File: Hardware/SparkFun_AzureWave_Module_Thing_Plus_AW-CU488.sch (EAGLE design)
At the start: 54 parts, among them J3 QWIIC_RA, J5 USB-C, Q1 2.5A/30V, U2 CP210X, U3 AP2112, U4 MCP73831, U5 TC7USB40MU

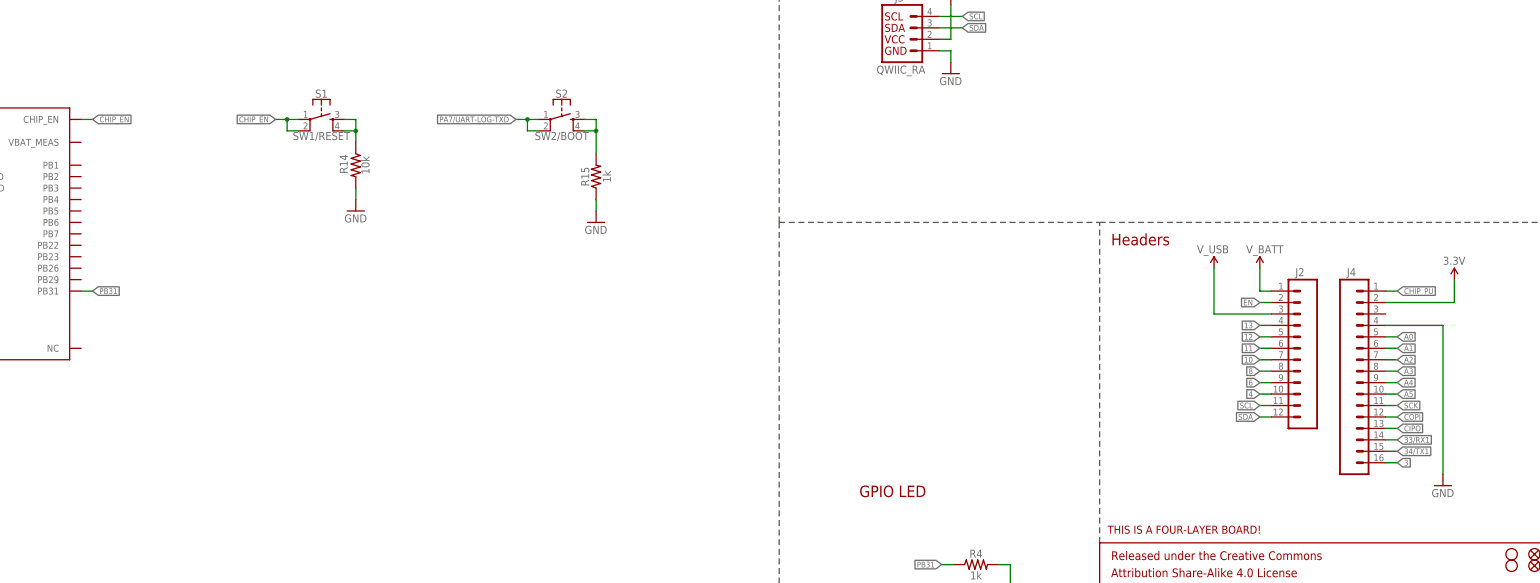
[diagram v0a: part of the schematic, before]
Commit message: vbat meas connection and some net cleanup
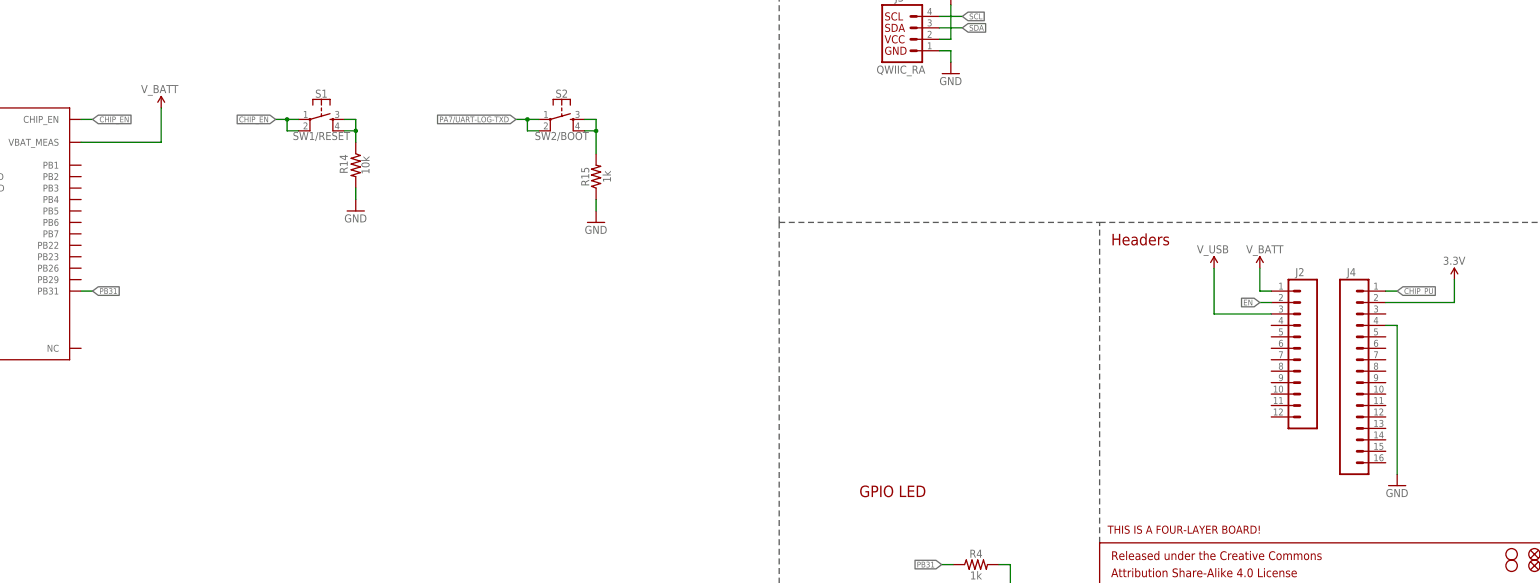
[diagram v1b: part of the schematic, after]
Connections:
- removed net 10: J2.7
- removed net 11: J2.6
- removed net 12: J2.5
- removed net 13: J2.4
- removed net 3: J4.16
- removed net 33/RX1: J4.14
- removed net 34/TX1: J4.15
- removed net 4: J2.10
- removed net 6: J2.9
- removed net 8: J2.8
- removed net A0: J4.5
- removed net A1: J4.6
- removed net A2: J4.7
- removed net A3: J4.8
- removed net A4: J4.9
- removed net A5: J4.10
- removed net CIPO: J4.13
- removed net COPI: J4.12
- removed net SCK: J4.11
- net SCL: no longer J2.11
- net SDA: no longer J2.12
- net V_BATT: now also U$13.VBAT_MEAS
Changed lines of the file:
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@@
 <part name="GND25" library="SparkFun-Aesthetics" deviceset="GND" device=""/>
 <part name="SUPPLY16" library="SparkFun-Aesthetics" deviceset="3.3V" device=""/>
+<part name="SUPPLY13" library="SparkFun-Aesthetics" deviceset="V_BATT" device=""/>
 </parts>
 <sheets>
@@
 <attribute name="VALUE" x="406.4" y="97.282" size="1.778" layer="96" font="vector"/>
 </instance>
-<instance part="GND2" gate="1" x="406.4" y="48.26" smashed="yes">
-<attribute name="VALUE" x="403.86" y="45.72" size="1.778" layer="96" font="vector"/>
+<instance part="GND2" gate="1" x="396.24" y="48.26" smashed="yes">
+<attribute name="VALUE" x="393.7" y="45.72" size="1.778" layer="96" font="vector"/>
 </instance>
 <instance part="C1" gate="G$1" x="101.6" y="226.06" smashed="yes">
@@
 <instance part="SUPPLY16" gate="G$1" x="45.72" y="144.78" smashed="yes">
 <attribute name="VALUE" x="44.704" y="148.336" size="1.778" layer="96" font="vector"/>
+</instance>
+<instance part="SUPPLY13" gate="G$1" x="121.92" y="132.08" smashed="yes" rot="MR0">
+<attribute name="VALUE" x="125.73" y="135.382" size="1.778" layer="96" font="vector" rot="MR0"/>
 </instance>
 </instances>
@@
 <pinref part="J4" gate="G$1" pin="4"/>
 <pinref part="GND2" gate="1" pin="GND"/>
-<wire x1="393.7" y1="83.82" x2="406.4" y2="83.82" width="0.1524" layer="91"/>
-<wire x1="406.4" y1="83.82" x2="406.4" y2="50.8" width="0.1524" layer="91"/>
+<wire x1="393.7" y1="83.82" x2="396.24" y2="83.82" width="0.1524" layer="91"/>
+<wire x1="396.24" y1="83.82" x2="396.24" y2="50.8" width="0.1524" layer="91"/>
 </segment>
 <segment>
@@
 <wire x1="365.76" y1="91.44" x2="365.76" y2="96.52" width="0.1524" layer="91"/>
 </segment>
+<segment>
+<pinref part="SUPPLY13" gate="G$1" pin="V_BATT"/>
+<wire x1="121.92" y1="132.08" x2="121.92" y2="124.46" width="0.1524" layer="91"/>
+<pinref part="U$13" gate="G$1" pin="VBAT_MEAS"/>
+<wire x1="121.92" y1="124.46" x2="104.14" y2="124.46" width="0.1524" layer="91"/>
+</segment>
 </net>
 <net name="N$1" class="0">
@@
 </segment>
 </net>
-<net name="A0" class="0">
-<segment>
-<pinref part="J4" gate="G$1" pin="5"/>
-<wire x1="393.7" y1="81.28" x2="396.24" y2="81.28" width="0.1524" layer="91"/>
-<label x="396.24" y="81.28" size="1.27" layer="95" font="vector" xref="yes"/>
-</segment>
-</net>
-<net name="A1" class="0">
-<segment>
-<pinref part="J4" gate="G$1" pin="6"/>
-<wire x1="393.7" y1="78.74" x2="396.24" y2="78.74" width="0.1524" layer="91"/>
-<label x="396.24" y="78.74" size="1.27" layer="95" font="vector" xref="yes"/>
-</segment>
-</net>
-<net name="A2" class="0">
-<segment>
-<pinref part="J4" gate="G$1" pin="7"/>
-<wire x1="393.7" y1="76.2" x2="396.24" y2="76.2" width="0.1524" layer="91"/>
-<label x="396.24" y="76.2" size="1.27" layer="95" font="vector" xref="yes"/>
-</segment>
-</net>
-<net name="A3" class="0">
-<segment>
-<pinref part="J4" gate="G$1" pin="8"/>
-<wire x1="393.7" y1="73.66" x2="396.24" y2="73.66" width="0.1524" layer="91"/>
-<label x="396.24" y="73.66" size="1.27" layer="95" font="vector" xref="yes"/>
-</segment>
-</net>
-<net name="A4" class="0">
-<segment>
-<pinref part="J4" gate="G$1" pin="9"/>
-<wire x1="393.7" y1="71.12" x2="396.24" y2="71.12" width="0.1524" layer="91"/>
-<label x="396.24" y="71.12" size="1.27" layer="95" font="vector" xref="yes"/>
-</segment>
-</net>
-<net name="A5" class="0">
-<segment>
-<pinref part="J4" gate="G$1" pin="10"/>
-<wire x1="393.7" y1="68.58" x2="396.24" y2="68.58" width="0.1524" layer="91"/>
-<label x="396.24" y="68.58" size="1.27" layer="95" font="vector" xref="yes"/>
-</segment>
-</net>
-<net name="SCK" class="0">
-<segment>
-<pinref part="J4" gate="G$1" pin="11"/>
-<wire x1="393.7" y1="66.04" x2="396.24" y2="66.04" width="0.1524" layer="91"/>
-<label x="396.24" y="66.04" size="1.27" layer="95" font="vector" xref="yes"/>
-</segment>
-</net>
-<net name="COPI" class="0">
-<segment>
-<pinref part="J4" gate="G$1" pin="12"/>
-<wire x1="393.7" y1="63.5" x2="396.24" y2="63.5" width="0.1524" layer="91"/>
-<label x="396.24" y="63.5" size="1.27" layer="95" font="vector" xref="yes"/>
-</segment>
-</net>
-<net name="CIPO" class="0">
-<segment>
-<pinref part="J4" gate="G$1" pin="13"/>
-<wire x1="393.7" y1="60.96" x2="396.24" y2="60.96" width="0.1524" layer="91"/>
-<label x="396.24" y="60.96" size="1.27" layer="95" font="vector" xref="yes"/>
-</segment>
-</net>
 <net name="SDA" class="0">
-<segment>
-<pinref part="J2" gate="G$1" pin="12"/>
-<wire x1="368.3" y1="63.5" x2="365.76" y2="63.5" width="0.1524" layer="91"/>
-<label x="365.76" y="63.5" size="1.27" layer="95" font="vector" rot="R180" xref="yes"/>
-</segment>
 <segment>
 <pinref part="J3" gate="G$1" pin="3"/>
@@
 <net name="SCL" class="0">
 <segment>
-<pinref part="J2" gate="G$1" pin="11"/>
-<wire x1="368.3" y1="66.04" x2="365.76" y2="66.04" width="0.1524" layer="91"/>
-<label x="365.76" y="66.04" size="1.27" layer="95" font="vector" rot="R180" xref="yes"/>
-</segment>
-<segment>
 <pinref part="J3" gate="G$1" pin="4"/>
 <wire x1="294.64" y1="152.4" x2="299.72" y2="152.4" width="0.1524" layer="91"/>
 <label x="299.72" y="152.4" size="1.27" layer="95" font="vector" xref="yes"/>
-</segment>
-</net>
-<net name="12" class="0">
-<segment>
-<pinref part="J2" gate="G$1" pin="5"/>
-<wire x1="368.3" y1="81.28" x2="365.76" y2="81.28" width="0.1524" layer="91"/>
-<label x="365.76" y="81.28" size="1.27" layer="95" font="vector" rot="R180" xref="yes"/>
-</segment>
-</net>
-<net name="13" class="0">
-<segment>
-<pinref part="J2" gate="G$1" pin="4"/>
-<wire x1="368.3" y1="83.82" x2="365.76" y2="83.82" width="0.1524" layer="91"/>
-<label x="365.76" y="83.82" size="1.27" layer="95" font="vector" rot="R180" xref="yes"/>
 </segment>
 </net>
@@
 </segment>
 </net>
-<net name="6" class="0">
-<segment>
-<pinref part="J2" gate="G$1" pin="9"/>
-<wire x1="368.3" y1="71.12" x2="365.76" y2="71.12" width="0.1524" layer="91"/>
-<label x="365.76" y="71.12" size="1.27" layer="95" font="vector" rot="R180" xref="yes"/>
-</segment>
-</net>
-<net name="8" class="0">
-<segment>
-<pinref part="J2" gate="G$1" pin="8"/>
-<wire x1="368.3" y1="73.66" x2="365.76" y2="73.66" width="0.1524" layer="91"/>
-<label x="365.76" y="73.66" size="1.27" layer="95" font="vector" rot="R180" xref="yes"/>
-</segment>
-</net>
-<net name="10" class="0">
-<segment>
-<pinref part="J2" gate="G$1" pin="7"/>
-<wire x1="368.3" y1="76.2" x2="365.76" y2="76.2" width="0.1524" layer="91"/>
-<label x="365.76" y="76.2" size="1.27" layer="95" font="vector" rot="R180" xref="yes"/>
-</segment>
-</net>
-<net name="11" class="0">
-<segment>
-<pinref part="J2" gate="G$1" pin="6"/>
-<wire x1="368.3" y1="78.74" x2="365.76" y2="78.74" width="0.1524" layer="91"/>
-<label x="365.76" y="78.74" size="1.27" layer="95" font="vector" rot="R180" xref="yes"/>
-</segment>
-</net>
 <net name="CP210X_D+" class="0">
 <segment>
@@
 </segment>
 </net>
-<net name="33/RX1" class="0">
-<segment>
-<pinref part="J4" gate="G$1" pin="14"/>
-<wire x1="393.7" y1="58.42" x2="396.24" y2="58.42" width="0.1524" layer="91"/>
-<label x="396.24" y="58.42" size="1.27" layer="95" font="vector" xref="yes"/>
-</segment>
-</net>
-<net name="34/TX1" class="0">
-<segment>
-<pinref part="J4" gate="G$1" pin="15"/>
-<wire x1="393.7" y1="55.88" x2="396.24" y2="55.88" width="0.1524" layer="91"/>
-<label x="396.24" y="55.88" size="1.27" layer="95" font="vector" xref="yes"/>
-</segment>
-</net>
-<net name="4" class="0">
-<segment>
-<pinref part="J2" gate="G$1" pin="10"/>
-<wire x1="368.3" y1="68.58" x2="365.76" y2="68.58" width="0.1524" layer="91"/>
-<label x="365.76" y="68.58" size="1.27" layer="95" font="vector" rot="R180" xref="yes"/>
-</segment>
-</net>
-<net name="3" class="0">
-<segment>
-<pinref part="J4" gate="G$1" pin="16"/>
-<wire x1="393.7" y1="53.34" x2="396.24" y2="53.34" width="0.1524" layer="91"/>
-<label x="396.24" y="53.34" size="1.27" layer="95" font="vector" xref="yes"/>
-</segment>
-</net>

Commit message: layout almost there
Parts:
- R10: device SparkFun-Resistors:100OHM-0603-1/10W-1% -> SparkFun-Resistors:100OHM-0402-TIGHT-1/16W-1%
- R15: device SparkFun-Resistors:1KOHM-0603-1/10W-1% -> SparkFun-Resistors:1KOHM-0402T-1/16W-1%
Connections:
- removed net CHIP_PU: J4.1
- removed net PB31: R4.1, U$13.PB31
- new net PA0: J4.14, U$13.PA0
- new net PA16: J2.10, U$13.PA16
- new net PA18: J2.9, U$13.PA18
- new net PA2: J4.16, U$13.PA2
- new net PA27: J2.8, U$13.PA27
- new net PA30: J2.7, U$13.PA30
- new net PA4: J4.15, U$13.PA4
- new net PB1: J2.5, U$13.PB1
- new net PB2: J2.6, U$13.PB2
- new net PB22/A4: J4.9, U$13.PB22
- new net PB23/A5: J4.10, U$13.PB23
- new net PB26/SCK: J4.11, U$13.PB26
- new net PB29/PICO: J4.12, U$13.PB29
- new net PB3: J2.4, R4.1, U$13.PB3
- new net PB31/POCI: J4.13, U$13.PB31
- new net PB4/A0: J4.5, U$13.PB4
- new net PB5/A1: J4.6, U$13.PB5
- new net PB6/A2: J4.7, U$13.PB6
- new net PB7/A3: J4.8, U$13.PB7
- net CHIP_EN: now also J4.1
- net SCL: now also J2.11, U$13.PA15
- net SDA: now also J2.12, U$13.PA14
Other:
- moved on the sheet: R16

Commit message: Layout done for proto v01
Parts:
- removed J2: (no value), SparkFun-Connectors:CONN_12SM_SQ_NO_SILK
- removed J4: (no value), SparkFun-Connectors:CONN_161X16_SM_SQ_NOSILK
- added J1: THING_PLUS, SparkFun-Boards:THING_PLUS
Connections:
- net 3.3V: now also J1.3V3; no longer J4.2
- net CHIP_EN: now also J1.!RESET; no longer J4.1
- net EN: now also J1.!EN; no longer J2.2
- net GND: now also J1.GND; no longer J4.4
- net PA0: now also J1.RX; no longer J4.14
- net PA16: now also J1.GPIO6; no longer J2.10
- net PA18: now also J1.GPIO5; no longer J2.9
- net PA2: now also J1.FREE; no longer J4.16
- net PA27: now also J1.GPIO4; no longer J2.8
- net PA30: now also J1.GPIO3; no longer J2.7
- net PA4: now also J1.TX; no longer J4.15
- net PB1: now also J1.GPIO1; no longer J2.5
- net PB2: now also J1.GPIO2; no longer J2.6
- net PB22/A4: now also J1.A4; no longer J4.9
- net PB23/A5: now also J1.A5; no longer J4.10
- net PB26/SCK: now also J1.SCK; no longer J4.11
- net PB29/PICO: now also J1.PICO; no longer J4.12
- net PB3: now also J1.GPIO0; no longer J2.4
- net PB31/POCI: now also J1.POCI; no longer J4.13
- net PB4/A0: now also J1.A0; no longer J4.5
- net PB5/A1: now also J1.A1; no longer J4.6
- net PB6/A2: now also J1.A2; no longer J4.7
- net PB7/A3: now also J1.A3; no longer J4.8
- net SCL: now also J1.SCL; no longer J2.11
- net SDA: now also J1.SDA; no longer J2.12
- net V_BATT: now also J1.VBAT; no longer J2.1
- net V_USB: now also J1.VUSB; no longer J2.3
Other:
- note added: "Analog Inputs"
- note added: "EN & BOOT Buttons"
- note added: "I2C"
- note added: "Native USB"
- note added: "SPI"
- note added: "Thing Plus Headers"
- note removed: "Headers"
- moved on the sheet: C1, C10, C19, C2, C3, C4, C6, C7, CHG, D1, D2, D3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

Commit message: tweaking for pin functions in progress
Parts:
- removed R2: 10k, SparkFun-Resistors:10KOHM-0402T-1/16W-1%
- removed U5: TC7USB40MU, esp32-s2-wroom:TC7USB40MU
- removed USB: JUMPER-SMT_3_1-NC_TRACE_SILK, SparkFun-Jumpers:JUMPER-SMT_3_1-NC_TRACE_SILK
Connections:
- removed net N$3: J5.D+, U5.D+
- removed net N$5: J5.D-, U5.D-
- removed net N$6: R2.2, USB.1
- removed net PA16: J1.GPIO6, U$13.PA16
- removed net PA18: J1.GPIO5, U$13.PA18
- removed net PB1: J1.GPIO1, U$13.PB1
- removed net PB2: J1.GPIO2, U$13.PB2
- removed net PB22/A4: J1.A4, U$13.PB22
- removed net PB23/A5: J1.A5, U$13.PB23
- removed net PB26/SCK: J1.SCK, U$13.PB26
- removed net PB29/PICO: J1.PICO, U$13.PB29
- removed net PB31/POCI: J1.POCI, U$13.PB31
- removed net PB5/A1: J1.A1, U$13.PB5
- removed net PB6/A2: J1.A2, U$13.PB6
- removed net USB_SEL: U5.S, USB.2
- new net PA16/PICO: J1.PICO, U$13.PA16/SPI0_PICO
- new net PA17/POCI: J1.POCI, U$13.PA17/SPI0_POCI
- new net PA18/SCK: J1.SCK, U$13.PA18/SPI0_CLK
- new net PA19/CS: J1.A5, U$13.PA19/SPI0_CS
- new net PB1/A4: J1.A2, U$13.PB1/ADC_4
- new net PB2/A5: J1.A3, U$13.PB2/ADC_5
- new net PB3/A6: J1.A4, U$13.PB3/ADC_6
- net 3.3V: no longer R2.1, U5.VCC
- net CP210X_D+: now also J5.D+; no longer U5.1D+
- net CP210X_D-: now also J5.D-; no longer U5.1D-
- net GND: no longer U5.!OE!, U5.GND, USB.3
- net PA0: no longer J1.RX
- net PA2: no longer J1.FREE
- net PA25/HSDM: no longer U5.2D-
- net PA26/HSDP: no longer U5.2D+
- net PA27: no longer J1.GPIO4
- net PA30: no longer J1.GPIO3
- net PA4: no longer J1.TX
- net PB3: no longer J1.GPIO0, U$13.PB3
- net PB4/A0: now also U$13.PB4/ADC_0; no longer U$13.PB4
- net PB7/A3: now also J1.A1, U$13.PB7/ADC_3; no longer J1.A3, U$13.PB7
- net SCL: now also U$13.PB5/ADC_1/LP_I2C_SCL; no longer U$13.PA15
- net SDA: now also U$13.PB6/ADC_2/LP_I2C_SDA; no longer U$13.PA14
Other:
- note removed: "Analog Inputs"
- note removed: "I2C"
- note removed: "Native USB"
- note removed: "SPI"
- note removed: "USB Jumper LOW: CP210X (default) HIGH: AW-CU488 native USB"
- moved on the sheet: C4, R16, U$13

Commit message: Routed but needs cleanup and silk updates
-added auto-reset back in
-broke out extra GPIO to "bonus" PTH headers on upper sides
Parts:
- added J2: (no value), SparkFun-Connectors:CONN_031X03_NO_SILK
- added J6: (no value), SparkFun-Connectors:CONN_021X02_NO_SILK
- added Q2: MBT3904DW1T1, SparkFun-DiscreteSemi:TRANS_NPN_DUAL-MBT3904DW1T1
- added R17, R18: 10k, SparkFun-Resistors:10KOHM-0402T-1/16W-1%
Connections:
- removed net PA25/HSDM: U$13.PA25/HSDM
- removed net PA26/HSDP: U$13.PA26/HSDP
- removed net PB3: R4.1
- new net DTR: Q2G2.E, R17.1, U2.DTR
- new net LP_UART_RXD: J1.RX, U$13.PA13/LP_UART_RXD
- new net LP_UART_TXD: J1.TX, U$13.PA12/LP_UART_TXD
- new net N$3: Q2G1.B, R17.2
- new net N$5: Q2G2.B, R18.2
- new net PA14: J6.1, U$13.PA14
- new net PA15: J6.2, U$13.PA15
- new net PB22: J1.GPIO2, U$13.PB22
- new net PB23: J1.GPIO3, U$13.PB23
- new net PB26: J1.GPIO1, U$13.PB26
- new net PB29: J1.GPIO0, R4.1, U$13.PB29
- new net PB31: J1.FREE, U$13.PB31
- new net PB5/A1: J1.A1, U$13.PB5/ADC_1/LP_I2C_SCL
- new net PB6/A2: J1.A2, U$13.PB6/ADC_2/LP_I2C_SDA
- new net RTS: Q2G1.E, R18.1, U2.RTS
- net CHIP_EN: now also Q2G1.C
- net PA0: now also J2.1
- net PA19/CS: now also J1.GPIO5; no longer J1.A5
- net PA2: now also J2.3
- net PA27: now also J1.GPIO4
- net PA30: now also J1.GPIO6
- net PA4: now also J2.2
- net PA7/UART-LOG-TXD: now also Q2G2.C, U$13.PA7/UART-LOG-TXD/DWNLD; no longer U$13.PA7/UART-LOG-TXD
- net PB1/A4: now also J1.A4; no longer J1.A2
- net PB2/A5: now also J1.A5; no longer J1.A3
- net PB3/A6: no longer J1.A4
- net PB7/A3: now also J1.A3; no longer J1.A1
- net SCL: now also U$13.PA25/HSDM/LP_I2C_SCL; no longer U$13.PB5/ADC_1/LP_I2C_SCL
- net SDA: now also U$13.PA26/HSDP/LP_I2C_SDA; no longer U$13.PB6/ADC_2/LP_I2C_SDA
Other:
- note added: "Auto program circuit DTR RTS EN LOG_TXD 1 1 1 1 0 0 1 1 1 0 0 1 0 1 1 0"
- note added: "Auto-Reset"
- moved on the sheet: C2, C3, J1, J5, R1, R11, R12, R5, R9, U2
